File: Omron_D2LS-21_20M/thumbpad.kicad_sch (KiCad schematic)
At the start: 15 parts, among them J1 Conn_01x10, SW1 D2LS-2120M, SW2 D2LS-2120M, SW3 D2LS-2120M, SW4 D2LS-2120M, U1 MAX6817, U2 MAX6817

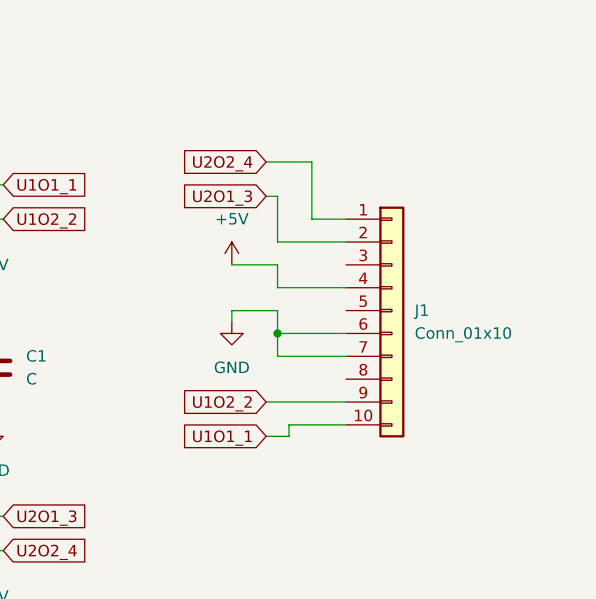
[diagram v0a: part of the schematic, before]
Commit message: 6pos connector added, board shrink
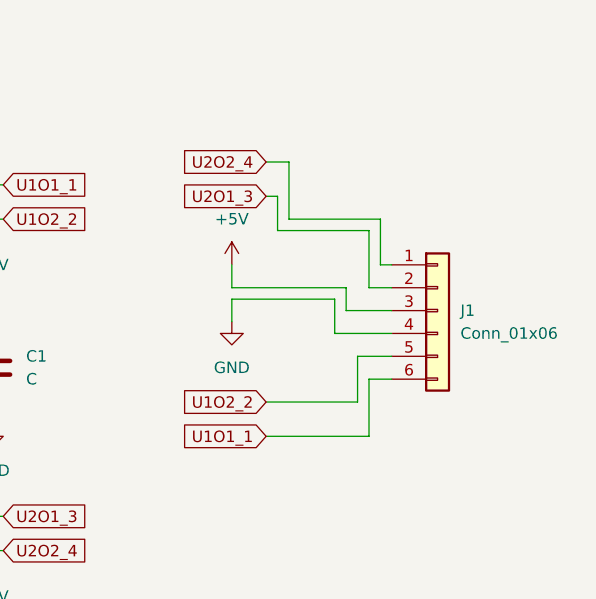
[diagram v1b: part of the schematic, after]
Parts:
- removed J1: Conn_01x10, Connector_FFC-FPC:TE_1-84952-0_1x10-1MP_P1.0mm_Horizontal, symbol Connector_Generic:Conn_01x10
- added J1: Conn_01x06, My_Library:TEAmp-CON6-84953-SMT-RA-FCC-FPC, symbol Connector_Generic:Conn_01x06
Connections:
- net +5V: now also J1.3 (Pin_3)
- net GND: now also J1.4 (Pin_4)
- net U1O1_1: now also J1.6 (Pin_6)
- net U1O2_2: now also J1.5 (Pin_5)
- net U2O1_3: now also J1.2 (Pin_2)
- net U2O2_4: now also J1.1 (Pin_1)
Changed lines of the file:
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@@
-	)
-	(junction
-		(at 185.42 59.69)
-		(diameter 0)
-		(color 0 0 0 0)
 	)
 	(junction
@@
 	(wire
 		(pts
-			(xy 193.04 46.99) (xy 189.23 46.99)
-		)
-		(stroke
-			(width 0)
-			(type default)
-		)
-	)
-	(wire
-		(pts
-			(xy 185.42 59.69) (xy 185.42 62.23)
+			(xy 186.69 46.99) (xy 196.85 46.99)
+		)
+		(stroke
+			(width 0)
+			(type default)
+		)
+	)
+	(wire
+		(pts
+			(xy 195.58 64.77) (xy 198.12 64.77)
 		)
 		(stroke
@@
 	(wire
 		(pts
-			(xy 180.34 58.42) (xy 180.34 57.15)
+			(xy 180.34 58.42) (xy 180.34 55.88)
+		)
+		(stroke
+			(width 0)
+			(type default)
+		)
+	)
+	(wire
+		(pts
+			(xy 195.58 71.12) (xy 195.58 64.77)
 		)
 		(stroke
@@
 	(wire
 		(pts
-			(xy 185.42 54.61) (xy 193.04 54.61)
-		)
-		(stroke
-			(width 0)
-			(type default)
-		)
-	)
-	(wire
-		(pts
 			(xy 66.04 114.3) (xy 78.74 114.3)
 		)
@@
 	(wire
 		(pts
-			(xy 184.15 40.64) (xy 189.23 40.64)
+			(xy 184.15 40.64) (xy 186.69 40.64)
+		)
+		(stroke
+			(width 0)
+			(type default)
+		)
+	)
+	(wire
+		(pts
+			(xy 196.85 52.07) (xy 198.12 52.07)
 		)
 		(stroke
@@
 	(wire
 		(pts
+			(xy 193.04 54.61) (xy 193.04 57.15)
+		)
+		(stroke
+			(width 0)
+			(type default)
+		)
+	)
+	(wire
+		(pts
 			(xy 149.86 53.34) (xy 149.86 46.99)
 		)
@@
 	(wire
 		(pts
+			(xy 180.34 54.61) (xy 180.34 52.07)
+		)
+		(stroke
+			(width 0)
+			(type default)
+		)
+	)
+	(wire
+		(pts
 			(xy 106.68 55.88) (xy 118.11 55.88)
 		)
@@
 	(wire
 		(pts
+			(xy 193.04 57.15) (xy 198.12 57.15)
+		)
+		(stroke
+			(width 0)
+			(type default)
+		)
+	)
+	(wire
+		(pts
 			(xy 153.67 93.98) (xy 153.67 95.25)
 		)
@@
 	(wire
 		(pts
-			(xy 185.42 44.45) (xy 185.42 49.53)
-		)
-		(stroke
-			(width 0)
-			(type default)
-		)
-	)
-	(wire
-		(pts
-			(xy 185.42 49.53) (xy 193.04 49.53)
+			(xy 185.42 44.45) (xy 185.42 48.26)
+		)
+		(stroke
+			(width 0)
+			(type default)
+		)
+	)
+	(wire
+		(pts
+			(xy 185.42 48.26) (xy 195.58 48.26)
 		)
 		(stroke
@@
 	(wire
 		(pts
-			(xy 180.34 57.15) (xy 185.42 57.15)
+			(xy 180.34 55.88) (xy 191.77 55.88)
 		)
 		(stroke
@@
 	(wire
 		(pts
-			(xy 185.42 59.69) (xy 193.04 59.69)
+			(xy 191.77 59.69) (xy 198.12 59.69)
 		)
 		(stroke
@@
 	(wire
 		(pts
-			(xy 186.69 71.12) (xy 186.69 69.85)
-		)
-		(stroke
-			(width 0)
-			(type default)
-		)
-	)
-	(wire
-		(pts
 			(xy 148.59 87.63) (xy 148.59 80.01)
 		)
@@
 	(wire
 		(pts
+			(xy 194.31 62.23) (xy 198.12 62.23)
+		)
+		(stroke
+			(width 0)
+			(type default)
+		)
+	)
+	(wire
+		(pts
 			(xy 148.59 50.8) (xy 148.59 43.18)
 		)
@@
 	(wire
 		(pts
-			(xy 185.42 52.07) (xy 185.42 54.61)
-		)
-		(stroke
-			(width 0)
-			(type default)
-		)
-	)
-	(wire
-		(pts
 			(xy 144.78 50.8) (xy 148.59 50.8)
 		)
@@
 	(wire
 		(pts
-			(xy 184.15 67.31) (xy 193.04 67.31)
-		)
-		(stroke
-			(width 0)
-			(type default)
-		)
-	)
-	(wire
-		(pts
-			(xy 189.23 40.64) (xy 189.23 46.99)
+			(xy 184.15 67.31) (xy 194.31 67.31)
+		)
+		(stroke
+			(width 0)
+			(type default)
+		)
+	)
+	(wire
+		(pts
+			(xy 195.58 48.26) (xy 195.58 54.61)
+		)
+		(stroke
+			(width 0)
+			(type default)
+		)
+	)
+	(wire
+		(pts
+			(xy 186.69 40.64) (xy 186.69 46.99)
 		)
 		(stroke
@@
 	(wire
 		(pts
-			(xy 180.34 52.07) (xy 185.42 52.07)
+			(xy 194.31 67.31) (xy 194.31 62.23)
+		)
+		(stroke
+			(width 0)
+			(type default)
+		)
+	)
+	(wire
+		(pts
+			(xy 180.34 54.61) (xy 193.04 54.61)
 		)
 		(stroke
@@
 	(wire
 		(pts
+			(xy 196.85 46.99) (xy 196.85 52.07)
+		)
+		(stroke
+			(width 0)
+			(type default)
+		)
+	)
+	(wire
+		(pts
 			(xy 144.78 87.63) (xy 148.59 87.63)
 		)
@@
 	(wire
 		(pts
-			(xy 185.42 62.23) (xy 193.04 62.23)
-		)
-		(stroke
-			(width 0)
-			(type default)
-		)
-	)
-	(wire
-		(pts
 			(xy 66.04 72.39) (xy 78.74 72.39)
 		)
@@
 	(wire
 		(pts
-			(xy 185.42 57.15) (xy 185.42 59.69)
+			(xy 191.77 55.88) (xy 191.77 59.69)
 		)
 		(stroke
@@
 	(wire
 		(pts
-			(xy 184.15 71.12) (xy 186.69 71.12)
-		)
-		(stroke
-			(width 0)
-			(type default)
-		)
-	)
-	(wire
-		(pts
-			(xy 186.69 69.85) (xy 193.04 69.85)
+			(xy 195.58 54.61) (xy 198.12 54.61)
+		)
+		(stroke
+			(width 0)
+			(type default)
+		)
+	)
+	(wire
+		(pts
+			(xy 184.15 71.12) (xy 195.58 71.12)
 		)
 		(stroke
@@
 	)
 	(symbol
-		(lib_id "Connector_Generic:Conn_01x10")
-		(at 198.12 57.15 0)
-		(unit 1)
-		(exclude_from_sim no)
-		(in_bom yes)
-		(on_board yes)
-		(dnp no)
-		(fields_autoplaced yes)
-		(property "Reference" "J1"
-			(at 200.66 57.1499 0)
-			(effects
-				(font
-					(size 1.27 1.27)
-				)
-				(justify left)
-			)
-		)
-		(property "Value" "Conn_01x10"
-			(at 200.66 59.6899 0)
-			(effects
-				(font
-					(size 1.27 1.27)
-				)
-				(justify left)
-			)
-		)
-		(property "Footprint" "Connector_FFC-FPC:TE_1-84952-0_1x10-1MP_P1.0mm_Horizontal"
-			(at 198.12 57.15 0)
-			(effects
-				(font
-					(size 1.27 1.27)
-				)
-				(hide yes)
-			)
-		)
-		(property "Datasheet" "~"
-			(at 198.12 57.15 0)
-			(effects
-				(font
-					(size 1.27 1.27)
-				)
-				(hide yes)
-			)
-		)
-		(property "Description" "Generic connector, single row, 01x10, script generated (kicad-library-utils/schlib/autogen/connector/)"
-			(at 198.12 57.15 0)
-			(effects
-				(font
-					(size 1.27 1.27)
-				)
-				(hide yes)
-			)
-		)
-		(pin "1"
-		)
-		(pin "8"
-		)
-		(pin "5"
-		)
-		(pin "4"
-		)
-		(pin "9"
-		)
-		(pin "6"
-		)
-		(pin "10"
-		)
-		(pin "3"
-		)
-		(pin "7"
-		)
-		(pin "2"
-		)
-		(instances
-			(project "thumbpad"
-				(path "/d46cfd13-8804-471a-abd6-4dc68ff59bf6"
-					(reference "J1")
-					(unit 1)
-				)
-			)
-		)
-	)
-	(symbol
 		(lib_id "power:GND")
 		(at 153.67 69.85 0)
@@
 					(unit 1)
 				)
+			)
+		)
+	)
+	(symbol
+		(lib_id "Connector_Generic:Conn_01x06")
+		(at 203.2 57.15 0)
+		(unit 1)
+		(exclude_from_sim no)
+		(in_bom yes)
+		(on_board yes)
+		(dnp no)
+		(fields_autoplaced yes)
+		(property "Reference" "J1"
+			(at 205.74 57.1499 0)
+			(effects
+				(font
+					(size 1.27 1.27)
+				)
+				(justify left)
+			)
+		)
+		(property "Value" "Conn_01x06"
+			(at 205.74 59.6899 0)
+			(effects
+				(font
+					(size 1.27 1.27)
+				)
+				(justify left)
+			)
+		)
+		(property "Footprint" "My_Library:TEAmp-CON6-84953-SMT-RA-FCC-FPC"
+			(at 203.2 57.15 0)
+			(effects
+				(font
+					(size 1.27 1.27)
+				)
+				(hide yes)
+			)
+		)
+		(property "Datasheet" "~"
+			(at 203.2 57.15 0)
+			(effects
+				(font
+					(size 1.27 1.27)
+				)
+				(hide yes)
+			)
+		)
+		(property "Description" "Generic connector, single row, 01x06, script generated (kicad-library-utils/schlib/autogen/connector/)"
+			(at 203.2 57.15 0)
+			(effects
+				(font
+					(size 1.27 1.27)
+				)
+				(hide yes)
+			)
+		)
+		(pin "3"
+		)
+		(pin "1"
+		)
+		(pin "5"
+		)
+		(pin "6"
+		)
+		(pin "2"
+		)
+		(pin "4"
+		)
+		(instances
+			(project "thumbpad"
+				(path "/d46cfd13-8804-471a-abd6-4dc68ff59bf6"
+					(reference "J1")
+					(unit 1)
+				)

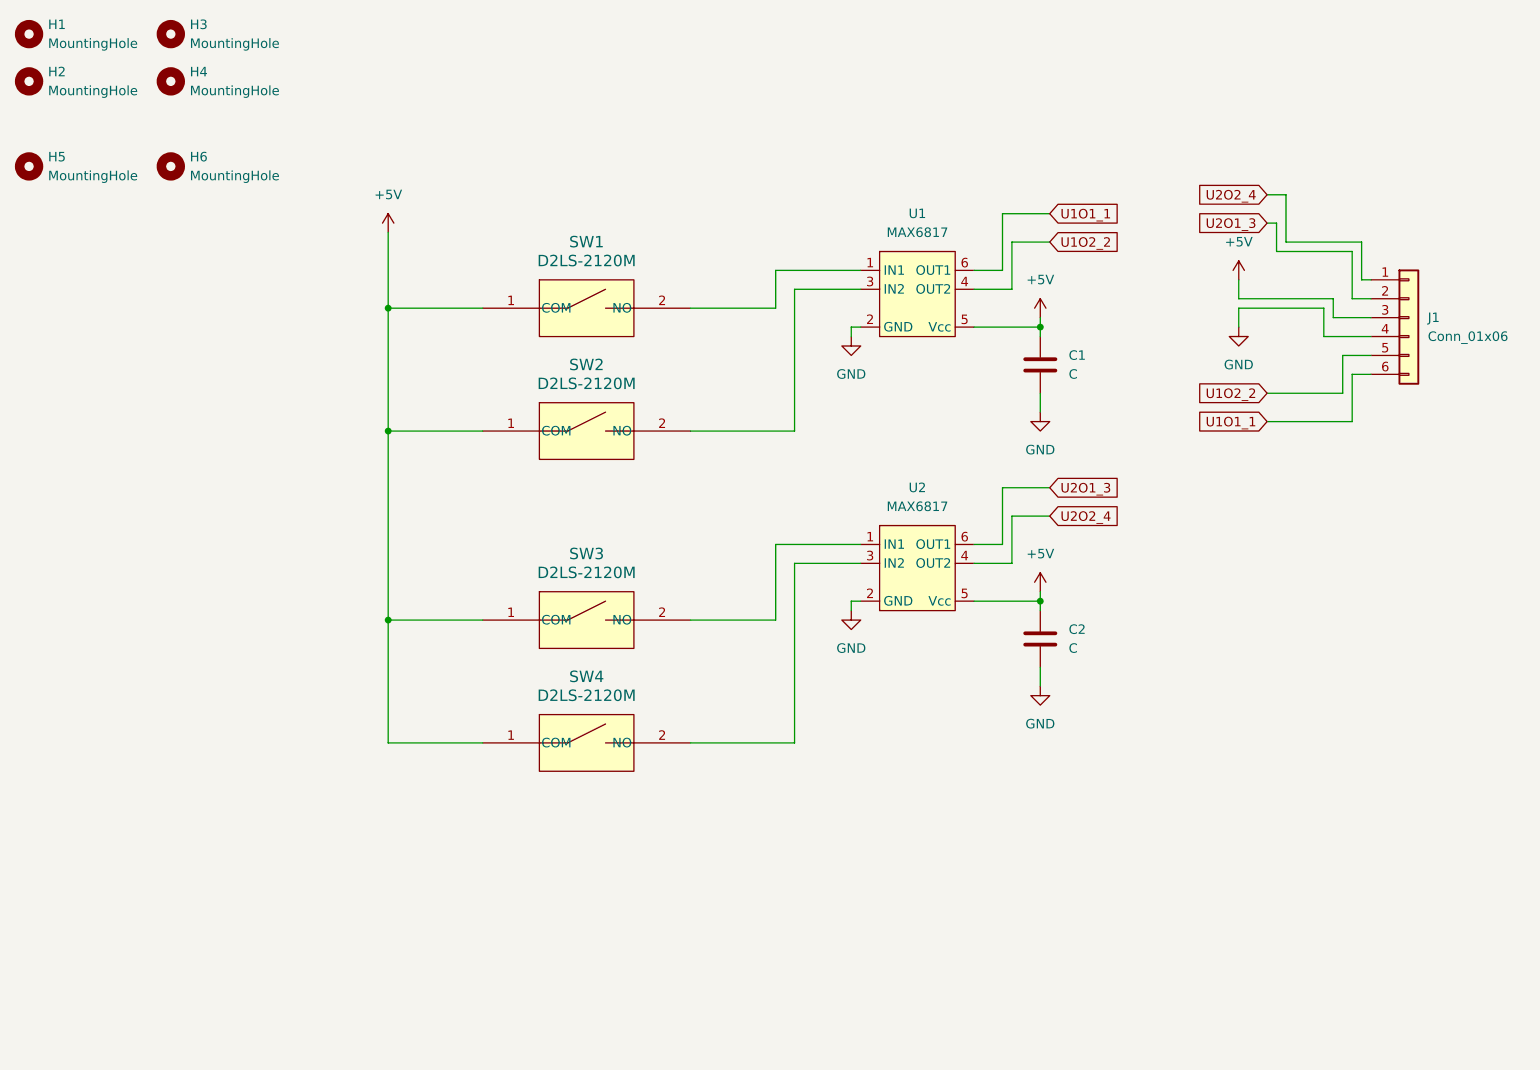
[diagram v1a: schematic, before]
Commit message: Added jumpers to bypass debouncers
Debouncing ICs are expensive, allows for software debounce option
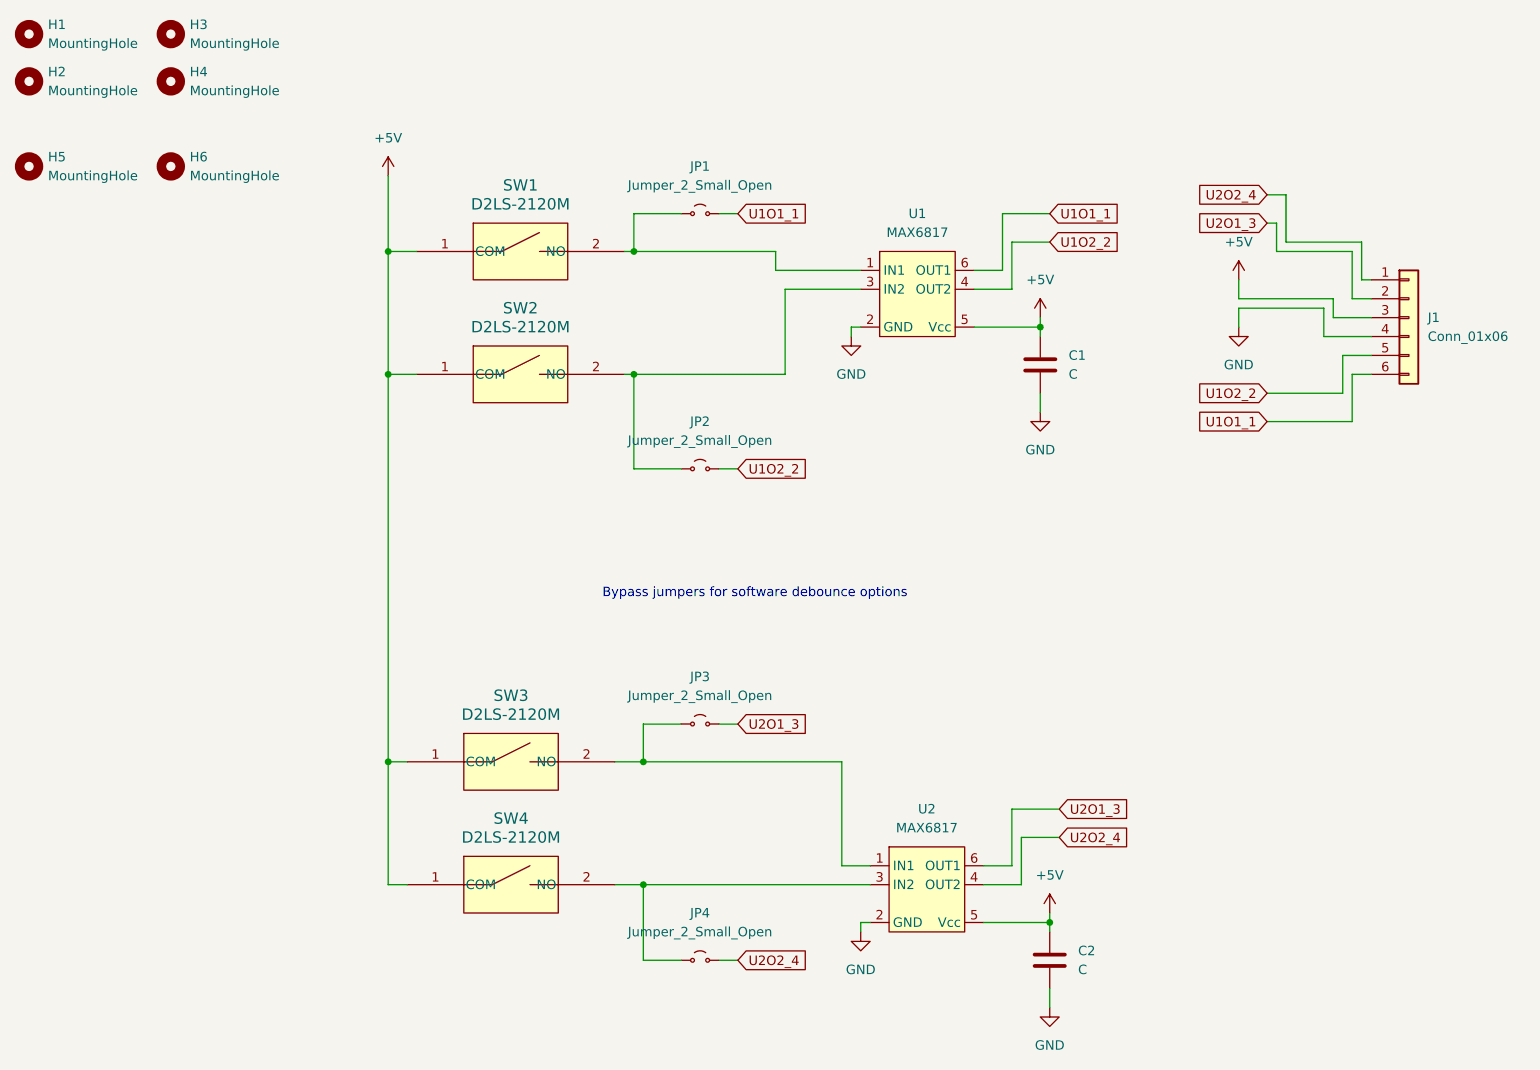
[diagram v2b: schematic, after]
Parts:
- added JP1, JP2, JP3, JP4: Jumper_2_Small_Open, Jumper:SolderJumper-2_P1.3mm_Open_Pad1.0x1.5mm, symbol Jumper:Jumper_2_Small_Open
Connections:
- net U1O1_1: now also JP1.2 (B)
- net U1O2_2: now also JP2.2 (B)
- net U2O1_3: now also JP3.2 (B)
- net U2O2_4: now also JP4.2 (B)
- net at SW3.2 (NO), U2.1 (IN1): now also JP3.1 (A)
- net at SW4.2 (NO), U2.3 (IN2): now also JP4.1 (A)
- net at SW1.2 (NO), U1.1 (IN1): now also JP1.1 (A)
- net at SW2.2 (NO), U1.3 (IN2): now also JP2.1 (A)
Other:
- note added: "Bypass jumpers for software debounce options"
- moved on the sheet: C2, SW1, SW2, SW3, SW4, U2
